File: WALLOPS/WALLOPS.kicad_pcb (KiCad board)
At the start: 2 copper layers, 55 x 68 mm, 28 parts, among them J1 JST-PH 1x9 Connector - WALLOP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, Q1 AO3401A, U1 VL53L8CX 0 (0x20; Zwicky), U2 VL58L8CX 1 (0x2A; Aristotle), U3 VL53L8CX 3 (0x2C; Copernicus), U4 VL53L8CX 2 (0x2B; Brahe), U5 6DOF IMU (0x69; Sisko), U6 5V to 3.3V Converter

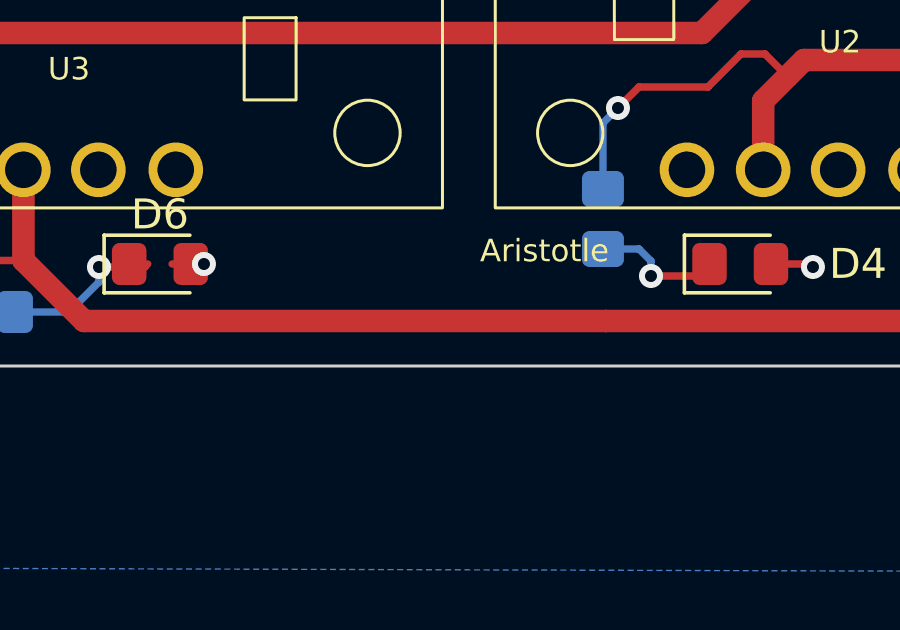
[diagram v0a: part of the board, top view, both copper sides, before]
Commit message: Added ATMOLiS logo to WALLOPS PCB
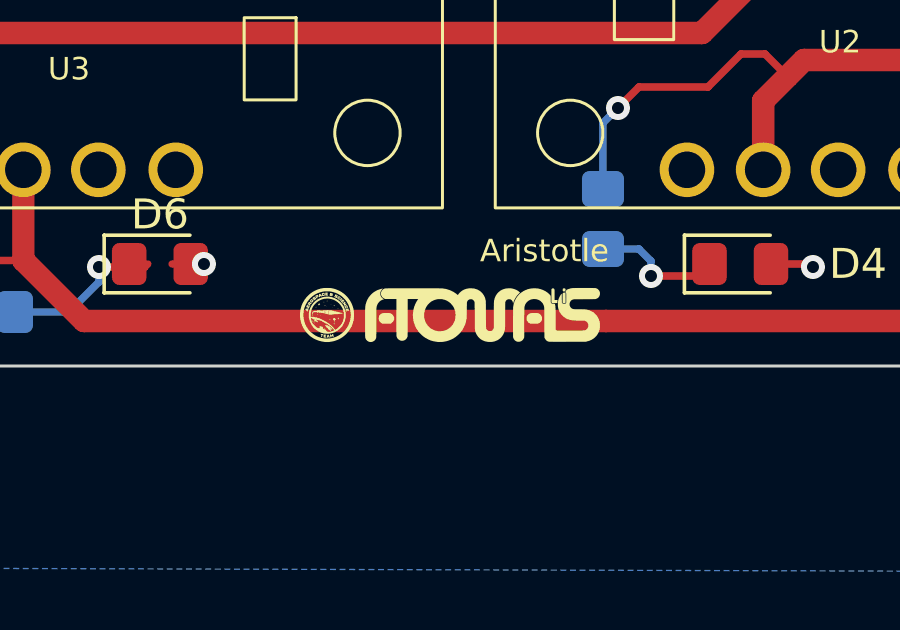
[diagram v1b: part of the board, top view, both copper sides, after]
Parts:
- added G***: LOGO, LOGO, F.Cu at (186.7, 103.3)
